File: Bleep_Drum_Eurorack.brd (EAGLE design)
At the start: 98.1 x 59.7 mm, 62 parts, among them IC1 MCP6002, IC2 78L05Z, IC3 ATMEGA328P, IC4 MCP4921, Q1 2N3904, Q2 2N3904, Q3 2N3904, Q4 2N3904

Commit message: R12=100kOhm.
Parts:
- R12: value 1M -> 100k
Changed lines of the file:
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@@
 <attribute name="VALUE" x="35.1536" y="24.9936" size="1.27" layer="27" ratio="10" rot="R270"/>
 </element>
-<element name="R12" library="rcl" package="0204V" value="1M" x="13.97" y="15.875" rot="R90"/>
+<element name="R12" library="rcl" package="0204V" value="100k" x="13.97" y="15.875" rot="R90"/>
 <element name="OUT_AUDIO" library="thonkiconn" package="WQP-PJ301M-12_JACK" value="WQP-PJ301M-12_JACK" x="7.62" y="12.7" smashed="yes" rot="R90">
 <attribute name="NAME" x="12.0904" y="7.9502" size="1.27" layer="21" rot="R180"/>

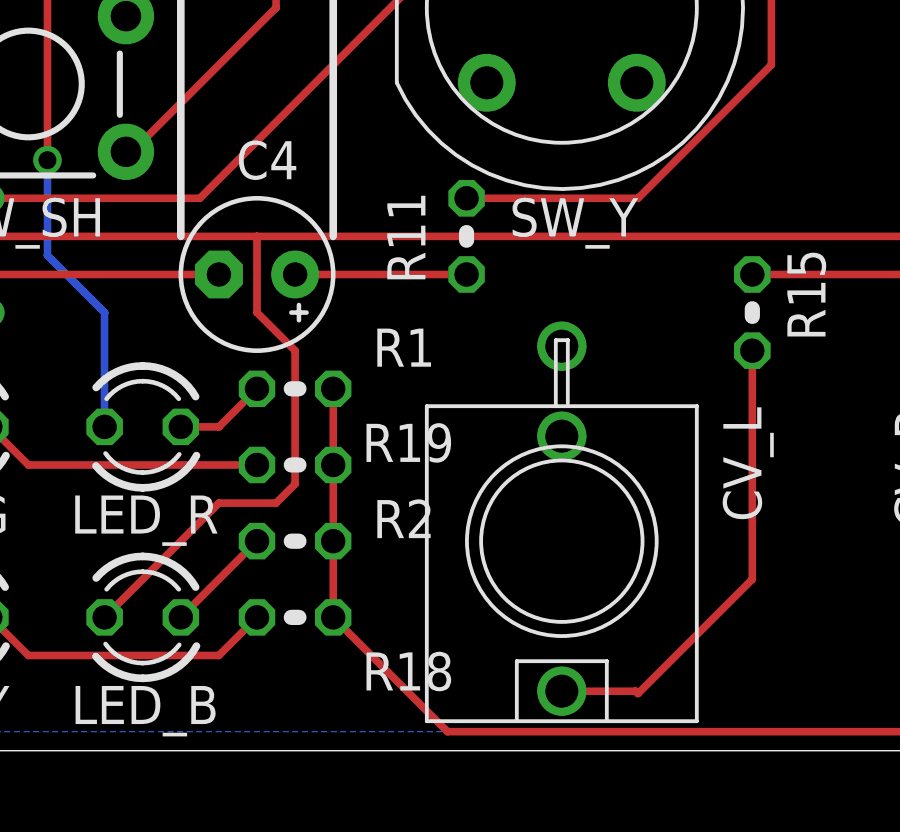
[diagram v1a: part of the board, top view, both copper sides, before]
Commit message: Moved R11 a bit. Moved a few component labels.
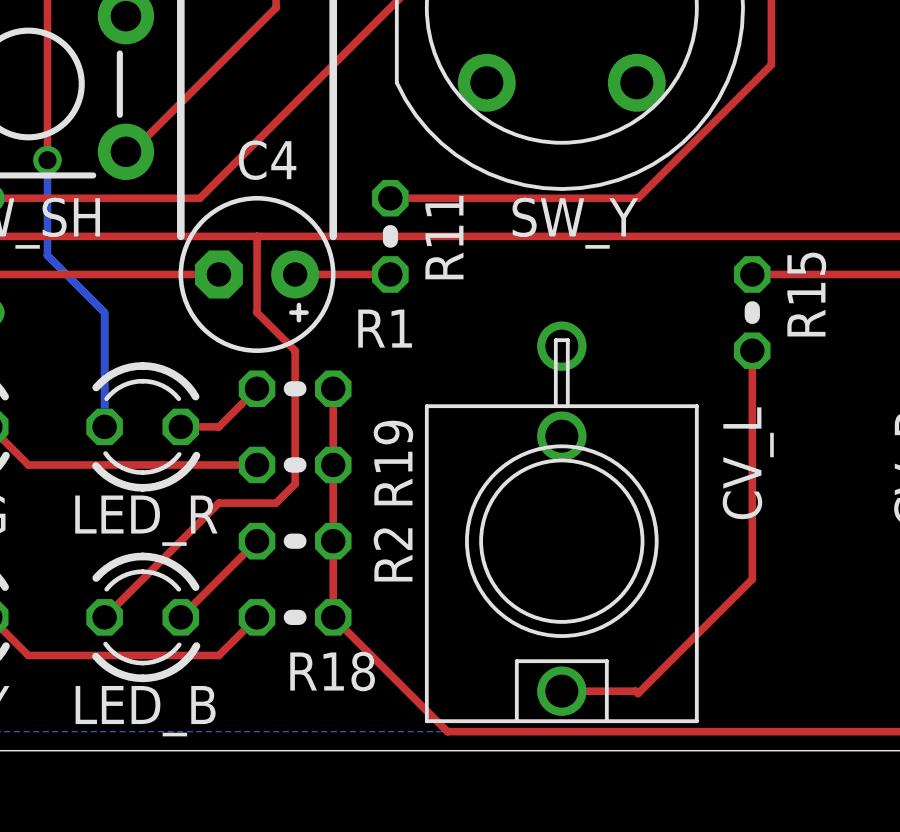
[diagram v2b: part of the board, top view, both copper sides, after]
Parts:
- moved R11 2.54 mm to (34.9, 22.9)
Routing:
- net N$2: track 83.3 -> 85.8 mm
- net N$1: track 5.72 -> 3.17 mm
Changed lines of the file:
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@@
 <attribute name="VALUE" x="17.145" y="55.88" size="1.27" layer="27" ratio="10" rot="R90"/>
 </element>
-<element name="R11" library="rcl" package="0204V" value="1k" x="37.465" y="22.86" smashed="yes" rot="R270">
-<attribute name="NAME" x="34.8234" y="24.3586" size="1.27" layer="25" ratio="10" rot="R270"/>
-<attribute name="VALUE" x="35.1536" y="24.9936" size="1.27" layer="27" ratio="10" rot="R270"/>
+<element name="R11" library="rcl" package="0204V" value="1k" x="34.925" y="22.86" smashed="yes" rot="R270">
+<attribute name="NAME" x="36.0934" y="24.3586" size="1.27" layer="25" ratio="10" rot="R270"/>
+<attribute name="VALUE" x="32.6136" y="24.9936" size="1.27" layer="27" ratio="10" rot="R270"/>
 </element>
 <element name="R12" library="rcl" package="0204V" value="100k" x="13.97" y="15.875" rot="R90"/>
@@
 </element>
 <element name="R1" library="rcl" package="0204V" value="10k" x="31.75" y="17.78" smashed="yes" rot="R180">
-<attribute name="NAME" x="36.4236" y="19.7866" size="1.27" layer="25" ratio="10" rot="R180"/>
+<attribute name="NAME" x="35.7886" y="20.4216" size="1.27" layer="25" ratio="10" rot="R180"/>
 <attribute name="VALUE" x="33.8836" y="20.0914" size="1.27" layer="27" ratio="10" rot="R180"/>
 </element>
@@
 </element>
 <element name="R2" library="rcl" package="0204V" value="10k" x="31.75" y="12.7" smashed="yes" rot="R180">
-<attribute name="NAME" x="36.4236" y="14.0716" size="1.27" layer="25" ratio="10" rot="R180"/>
+<attribute name="NAME" x="35.6616" y="11.2014" size="1.27" layer="25" ratio="10" rot="R90"/>
 <attribute name="VALUE" x="33.8836" y="15.0114" size="1.27" layer="27" ratio="10" rot="R180"/>
 </element>
@@
 </element>
 <element name="R18" library="rcl" package="0204V" value="10k" x="31.75" y="10.16" smashed="yes" rot="R180">
-<attribute name="NAME" x="37.0586" y="8.9916" size="1.27" layer="25" ratio="10" rot="R180"/>
+<attribute name="NAME" x="34.5186" y="8.9916" size="1.27" layer="25" ratio="10" rot="R180"/>
 <attribute name="VALUE" x="33.8836" y="12.4714" size="1.27" layer="27" ratio="10" rot="R180"/>
 </element>
@@
 </element>
 <element name="R19" library="rcl" package="0204V" value="10k" x="31.75" y="15.24" smashed="yes" rot="R180">
-<attribute name="NAME" x="37.0586" y="16.6116" size="1.27" layer="25" ratio="10" rot="R180"/>
+<attribute name="NAME" x="35.6616" y="13.7414" size="1.27" layer="25" ratio="10" rot="R90"/>
 <attribute name="VALUE" x="33.8836" y="17.5514" size="1.27" layer="27" ratio="10" rot="R180"/>
 </element>
@@
 <wire x1="87.63" y1="62.23" x2="86.36" y2="63.5" width="0.254" layer="1"/>
 <wire x1="86.36" y1="63.5" x2="69.215" y2="63.5" width="0.254" layer="1"/>
-<wire x1="43.18" y1="24.13" x2="37.465" y2="24.13" width="0.254" layer="1"/>
+<wire x1="43.18" y1="24.13" x2="34.925" y2="24.13" width="0.254" layer="1"/>
 </signal>
 <signal name="N$5">
@@
 <contactref element="R11" pad="2"/>
 <contactref element="C4" pad="+"/>
-<wire x1="31.75" y1="21.59" x2="37.465" y2="21.59" width="0.254" layer="1"/>
+<wire x1="31.75" y1="21.59" x2="34.925" y2="21.59" width="0.254" layer="1"/>
 </signal>
 <signal name="N$3">

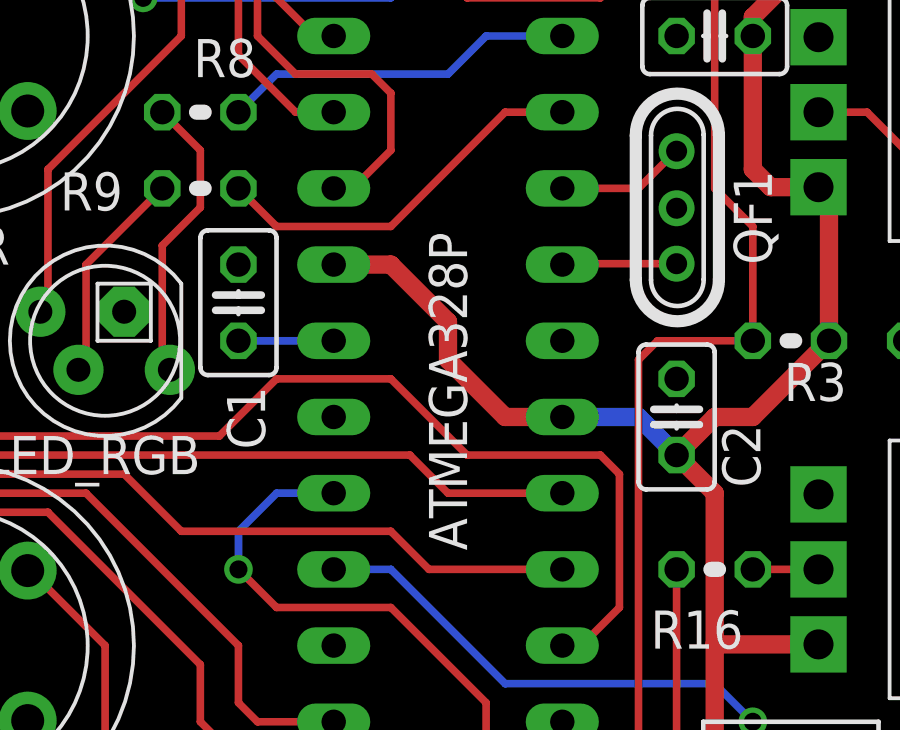
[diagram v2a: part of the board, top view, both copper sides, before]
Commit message: Changed ATmega328P into ATmega328. Arduino environment seems to expect the latter type (both work fine when programmed. It's just hard to get there with a "P" type chip :) ).
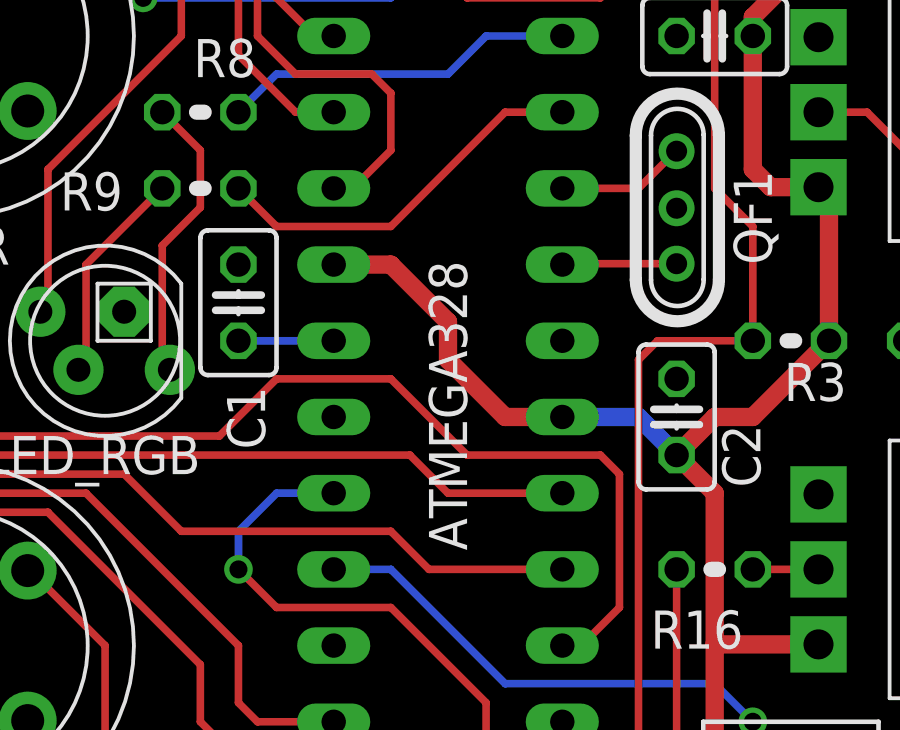
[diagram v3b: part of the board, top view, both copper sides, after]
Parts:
- IC3: value ATMEGA328P -> ATMEGA328
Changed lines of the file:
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@@
 <attribute name="NAME" x="6.3754" y="53.6702" size="1.27" layer="21" rot="R180"/>
 </element>
-<element name="IC3" library="SparkFun-DigitalIC" package="DIL28-3" value="ATMEGA328P" x="74.93" y="39.37" smashed="yes" rot="R90">
+<element name="IC3" library="SparkFun-DigitalIC" package="DIL28-3" value="ATMEGA328" x="74.93" y="39.37" smashed="yes" rot="R90">
 <attribute name="NAME" x="74.93" y="24.13" size="1.27" layer="25" ratio="10" rot="R90"/>
 <attribute name="VALUE" x="75.565" y="33.655" size="1.27" layer="25" ratio="10" rot="R90"/>
